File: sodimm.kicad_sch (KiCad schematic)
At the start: 2 parts, among them J9 2309409-1

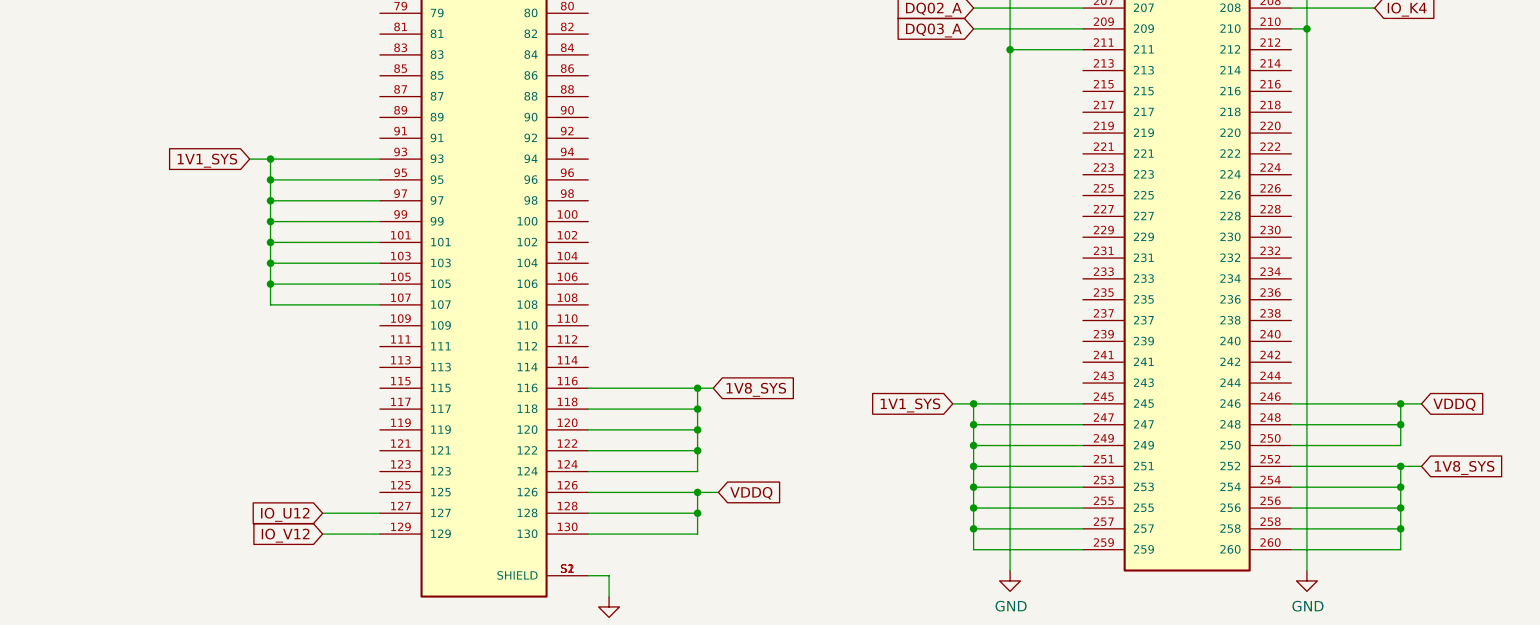
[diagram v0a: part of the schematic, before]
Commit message: Add DDR rail switches, update nets
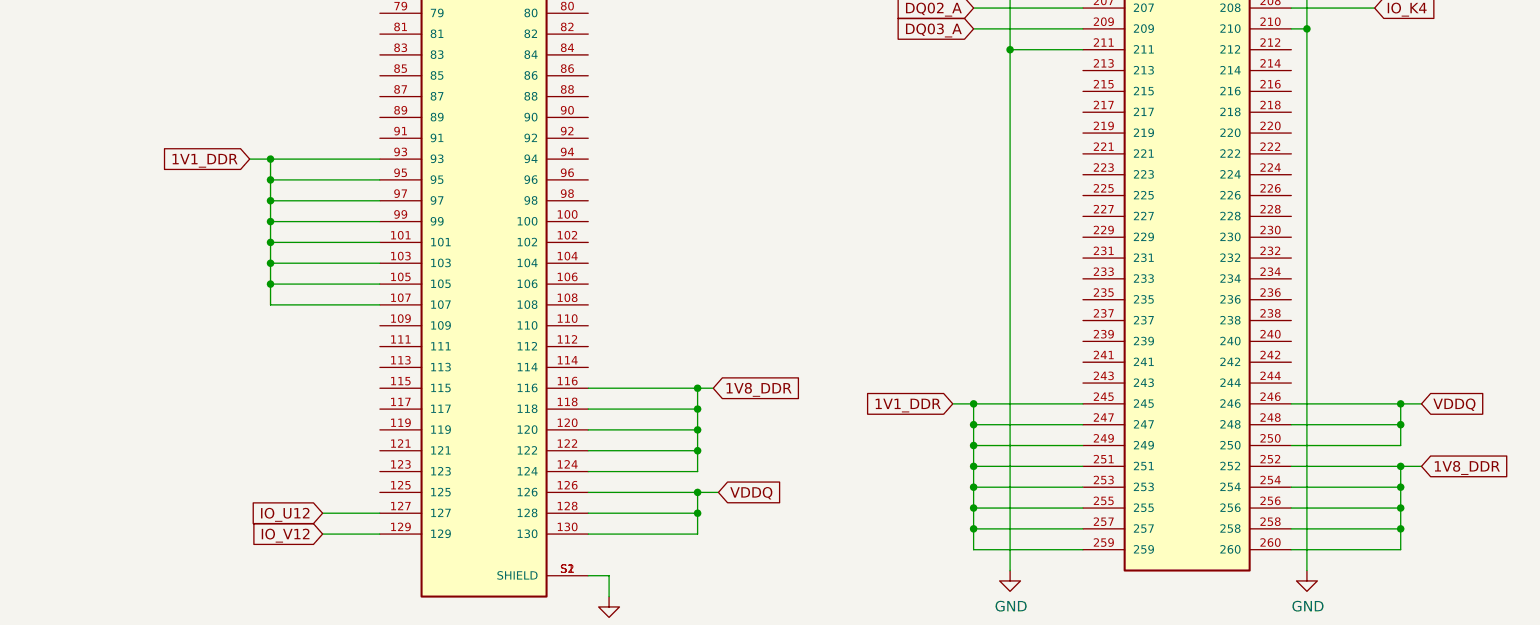
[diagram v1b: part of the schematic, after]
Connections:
- net 1V1_SYS renamed 1V1_DDR
- net 1V8_SYS renamed 1V8_DDR
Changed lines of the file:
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@@
+    )
+  )
+  (global_label "1V1_DDR" (shape input) (at 247.015 197.485 180) (fields_autoplaced)
+    (effects (font (size 1.27 1.27)) (justify right))
+    (property "Intersheet References" "${INTERSHEET_REFS}" (id 0) (at 236.4056 197.4056 0)
+      (effects (font (size 1.27 1.27)) (justify right) hide)
     )
   )
@@
     )
   )
-  (global_label "1V1_SYS" (shape input) (at 247.015 197.485 180) (fields_autoplaced)
-    (effects (font (size 1.27 1.27)) (justify right))
-    (property "Intersheet References" "${INTERSHEET_REFS}" (id 0) (at 0 0 0)
-      (effects (font (size 1.27 1.27)) hide)
-    )
-  )
   (global_label "DQ_S0_TA" (shape input) (at 250.19 141.605 180) (fields_autoplaced)
     (effects (font (size 1.27 1.27)) (justify right))
@@
     )
   )
+  (global_label "1V8_DDR" (shape input) (at 304.165 205.105 0) (fields_autoplaced)
+    (effects (font (size 1.27 1.27)) (justify left))
+    (property "Intersheet References" "${INTERSHEET_REFS}" (id 0) (at 314.7744 205.0256 0)
+      (effects (font (size 1.27 1.27)) (justify left) hide)
+    )
+  )
   (global_label "DQ_S1_TA" (shape input) (at 250.19 108.585 180) (fields_autoplaced)
     (effects (font (size 1.27 1.27)) (justify right))
@@
     )
   )
+  (global_label "1V8_DDR" (shape input) (at 217.805 195.58 0) (fields_autoplaced)
+    (effects (font (size 1.27 1.27)) (justify left))
+    (property "Intersheet References" "${INTERSHEET_REFS}" (id 0) (at 228.4144 195.5006 0)
+      (effects (font (size 1.27 1.27)) (justify left) hide)
+    )
+  )
   (global_label "IO_T4" (shape input) (at 298.45 113.665 0) (fields_autoplaced)
     (effects (font (size 1.27 1.27)) (justify left))
@@
     )
   )
+  (global_label "1V1_DDR" (shape input) (at 161.29 167.64 180) (fields_autoplaced)
+    (effects (font (size 1.27 1.27)) (justify right))
+    (property "Intersheet References" "${INTERSHEET_REFS}" (id 0) (at 150.6806 167.5606 0)
+      (effects (font (size 1.27 1.27)) (justify right) hide)
+    )
+  )
   (global_label "DQ09_A" (shape input) (at 250.825 98.425 180) (fields_autoplaced)
     (effects (font (size 1.27 1.27)) (justify right))
@@
     )
   )
-  (global_label "1V8_SYS" (shape input) (at 217.805 195.58 0) (fields_autoplaced)
-    (effects (font (size 1.27 1.27)) (justify left))
-    (property "Intersheet References" "${INTERSHEET_REFS}" (id 0) (at 0 0 0)
-      (effects (font (size 1.27 1.27)) hide)
-    )
-  )
   (global_label "CKE0_A" (shape input) (at 298.45 133.985 0) (fields_autoplaced)
     (effects (font (size 1.27 1.27)) (justify left))
@@
     )
   )
-  (global_label "1V8_SYS" (shape input) (at 304.165 205.105 0) (fields_autoplaced)
-    (effects (font (size 1.27 1.27)) (justify left))
-    (property "Intersheet References" "${INTERSHEET_REFS}" (id 0) (at 0 0 0)
-      (effects (font (size 1.27 1.27)) hide)
-    )
-  )
   (global_label "DMI_1A" (shape input) (at 250.19 103.505 180) (fields_autoplaced)
     (effects (font (size 1.27 1.27)) (justify right))
     (property "Intersheet References" "${INTERSHEET_REFS}" (id 0) (at 0 0 0)
-      (effects (font (size 1.27 1.27)) hide)
-    )
-  )
-  (global_label "1V1_SYS" (shape input) (at 161.29 167.64 180) (fields_autoplaced)
-    (effects (font (size 1.27 1.27)) (justify right))
-    (property "Intersheet References" "${INTERSHEET_REFS}" (id 0) (at 0 0 0)

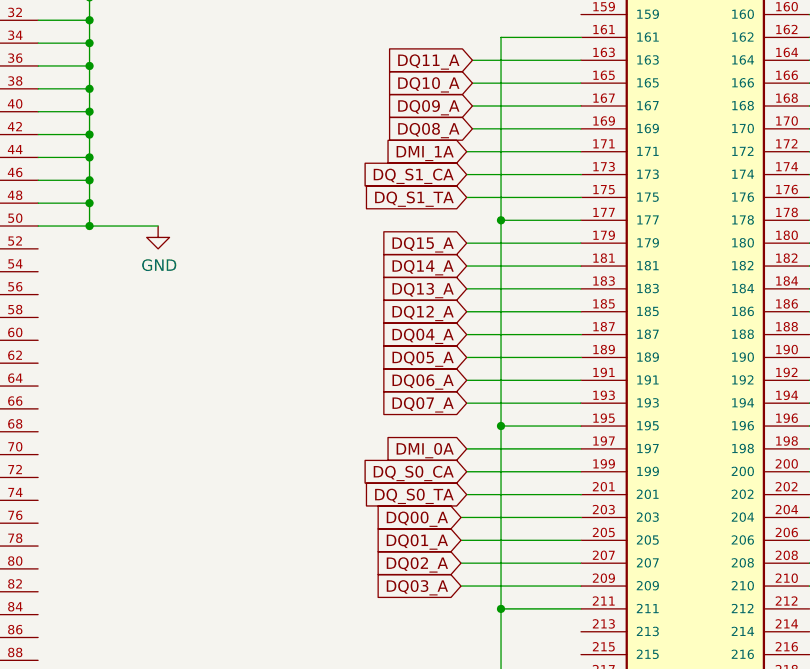
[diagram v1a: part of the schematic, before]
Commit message: DQS differential pairs renamed to be correctly recognized by KiCad, Created DQ and DQS class, DQ8-11 + DQ_S1 routed and matched with corrected class net parameters
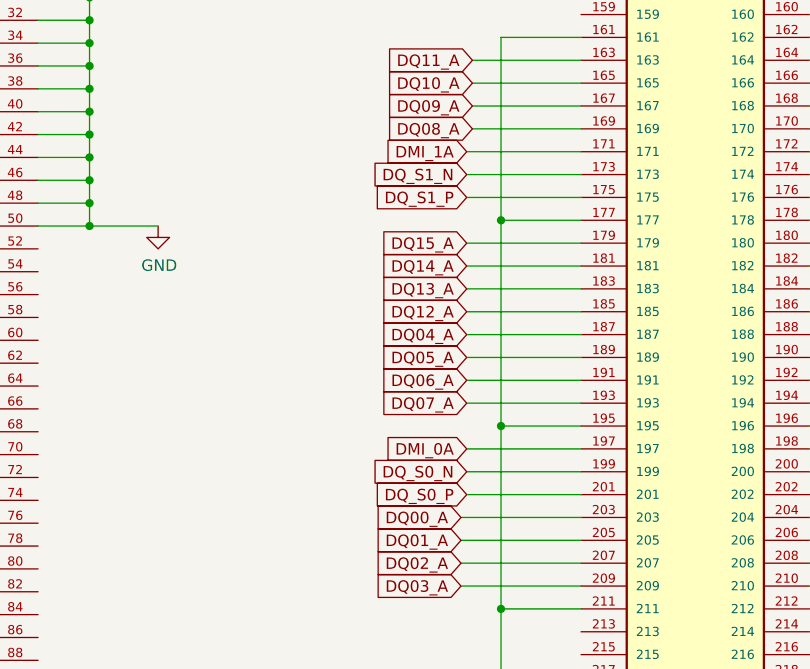
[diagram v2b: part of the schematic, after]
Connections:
- net DQ_S0_CA renamed DQ_S0_N
- net DQ_S0_TA renamed DQ_S0_P
- net DQ_S1_CA renamed DQ_S1_N
- net DQ_S1_TA renamed DQ_S1_P
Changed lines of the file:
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@@
     )
   )
-  (global_label "DQ_S0_TA" (shape input) (at 250.19 141.605 180) (fields_autoplaced)
-    (effects (font (size 1.27 1.27)) (justify right))
-    (property "Intersheet References" "${INTERSHEET_REFS}" (id 0) (at 0 0 0)
-      (effects (font (size 1.27 1.27)) hide)
+  (global_label "DQ_S0_P" (shape input) (at 250.19 141.605 180) (fields_autoplaced)
+    (effects (font (size 1.27 1.27)) (justify right))
+    (property "Intersheet References" "${INTERSHEET_REFS}" (id 0) (at 239.641 141.5256 0)
+      (effects (font (size 1.27 1.27)) (justify right) hide)
     )
   )
@@
     )
   )
-  (global_label "DQ_S1_TA" (shape input) (at 250.19 108.585 180) (fields_autoplaced)
-    (effects (font (size 1.27 1.27)) (justify right))
-    (property "Intersheet References" "${INTERSHEET_REFS}" (id 0) (at 0 0 0)
-      (effects (font (size 1.27 1.27)) hide)
+  (global_label "DQ_S1_P" (shape input) (at 250.19 108.585 180) (fields_autoplaced)
+    (effects (font (size 1.27 1.27)) (justify right))
+    (property "Intersheet References" "${INTERSHEET_REFS}" (id 0) (at 239.641 108.5056 0)
+      (effects (font (size 1.27 1.27)) (justify right) hide)
     )
   )
@@
     )
   )
-  (global_label "DQ_S0_CA" (shape input) (at 250.19 139.065 180) (fields_autoplaced)
-    (effects (font (size 1.27 1.27)) (justify right))
-    (property "Intersheet References" "${INTERSHEET_REFS}" (id 0) (at 0 0 0)
-      (effects (font (size 1.27 1.27)) hide)
+  (global_label "DQ_S0_N" (shape input) (at 250.19 139.065 180) (fields_autoplaced)
+    (effects (font (size 1.27 1.27)) (justify right))
+    (property "Intersheet References" "${INTERSHEET_REFS}" (id 0) (at 239.5806 138.9856 0)
+      (effects (font (size 1.27 1.27)) (justify right) hide)
     )
   )
@@
     )
   )
-  (global_label "DQ_S1_CA" (shape input) (at 250.19 106.045 180) (fields_autoplaced)
-    (effects (font (size 1.27 1.27)) (justify right))
-    (property "Intersheet References" "${INTERSHEET_REFS}" (id 0) (at 0 0 0)
-      (effects (font (size 1.27 1.27)) hide)
-    )
-  )
+  (global_label "DQ_S1_N" (shape input) (at 250.19 106.045 180) (fields_autoplaced)
+    (effects (font (size 1.27 1.27)) (justify right))
+    (property "Intersheet References" "${INTERSHEET_REFS}" (id 0) (at 239.5806 105.9656 0)
+      (effects (font (size 1.27 1.27)) (justify right) hide)
+    )
+  )

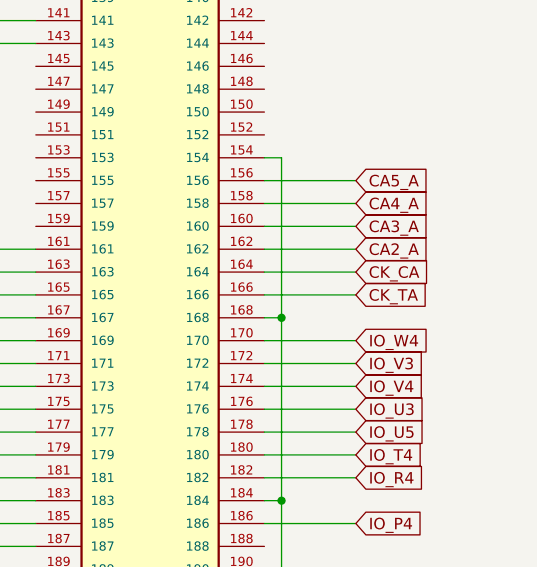
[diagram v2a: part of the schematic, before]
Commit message: Update name of CLK nets
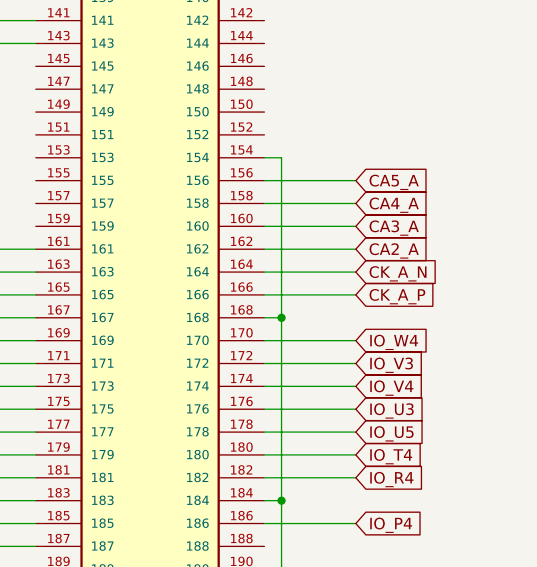
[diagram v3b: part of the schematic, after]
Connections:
- net CK_CA renamed CK_A_N
- net CK_TA renamed CK_A_P
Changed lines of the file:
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@@
     )
   )
-  (global_label "CK_CA" (shape input) (at 298.45 93.345 0) (fields_autoplaced)
+  (global_label "CK_A_N" (shape input) (at 298.45 93.345 0) (fields_autoplaced)
     (effects (font (size 1.27 1.27)) (justify left))
-    (property "Intersheet References" "${INTERSHEET_REFS}" (id 0) (at 0 0 0)
-      (effects (font (size 1.27 1.27)) hide)
+    (property "Intersheet References" "${INTERSHEET_REFS}" (id 0) (at 307.6685 93.2656 0)
+      (effects (font (size 1.27 1.27)) (justify left) hide)
     )
   )
@@
     )
   )
-  (global_label "CK_TA" (shape input) (at 298.45 95.885 0) (fields_autoplaced)
+  (global_label "CK_A_P" (shape input) (at 298.45 95.885 0) (fields_autoplaced)
     (effects (font (size 1.27 1.27)) (justify left))
-    (property "Intersheet References" "${INTERSHEET_REFS}" (id 0) (at 0 0 0)
-      (effects (font (size 1.27 1.27)) hide)
+    (property "Intersheet References" "${INTERSHEET_REFS}" (id 0) (at 307.608 95.8056 0)
+      (effects (font (size 1.27 1.27)) (justify left) hide)
     )
   )
